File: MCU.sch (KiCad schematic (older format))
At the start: 46 parts, among them J12 Conn_02x05_Odd_Even, Q28 LBSS84LT1G, SW3 SW_Push, SW4 SW_Push, U10 ESP32-WROOM-32U, U16 CH340G, U6 STM32F730R8T6, U7 LY68L6400SLIT, U9 FS35ND01G-S1Y2QWFI000, Y1 Q13FC1350000400, Y2 24MHz, Y3 12MHz

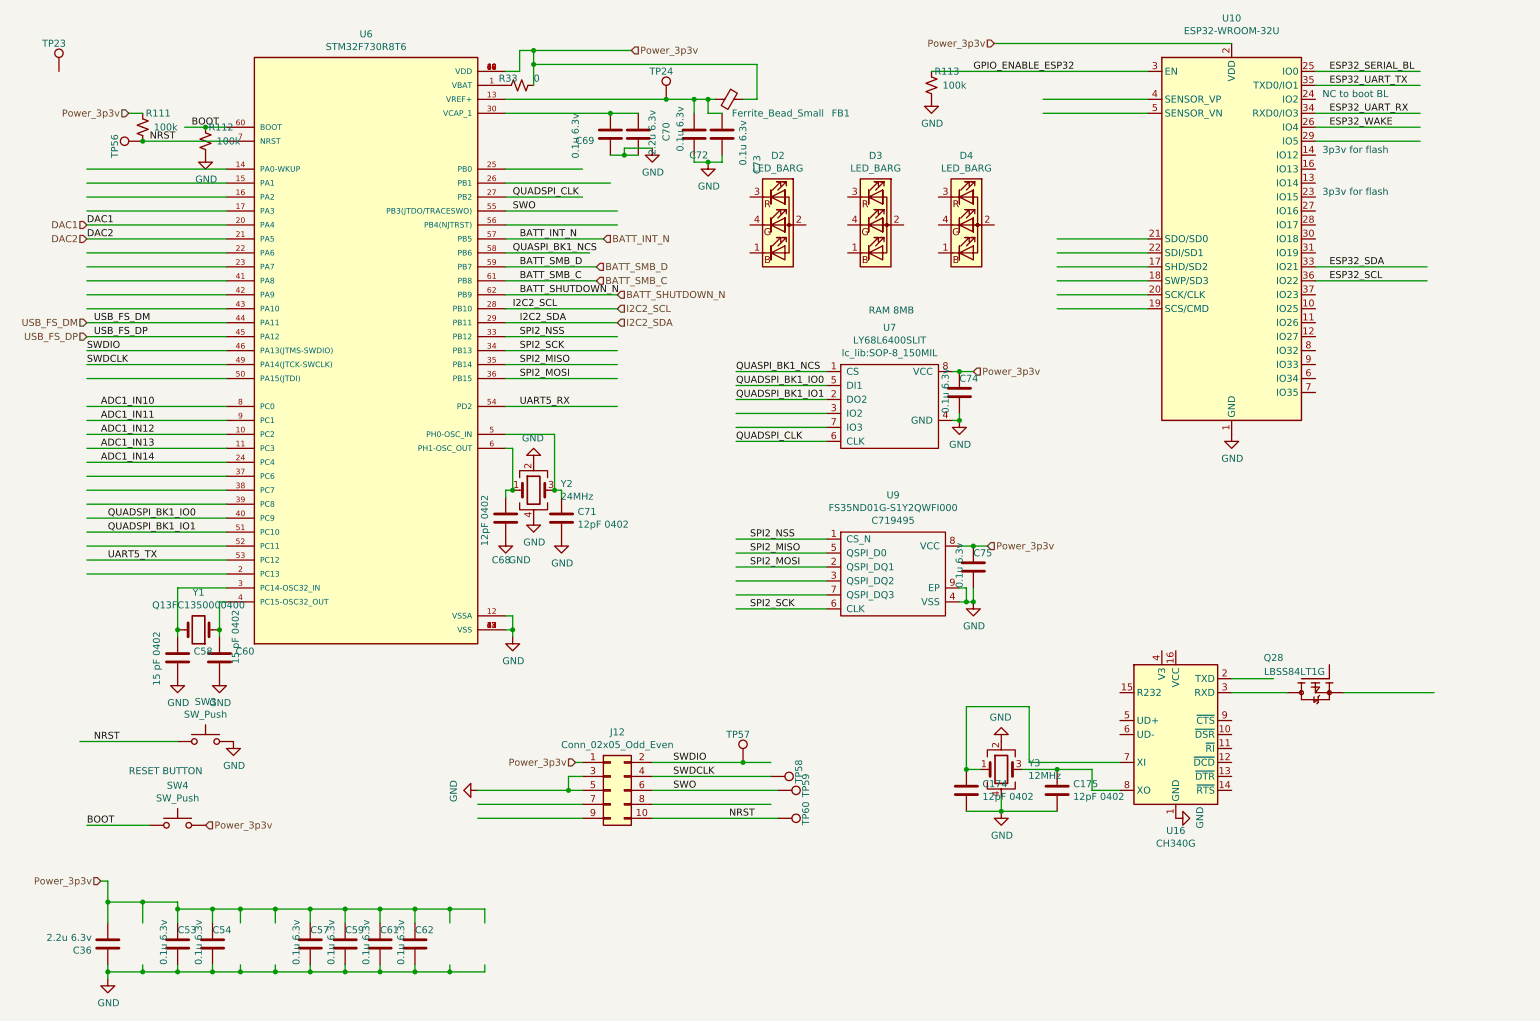
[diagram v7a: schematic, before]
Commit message: lots of GPIO connectivity changes. fixed no PD on input fixed CH340G leakage. can otherwise power from GPIO. added fet for powering VCONN from 3v/5v NEED TO ADD OVERCURRENT
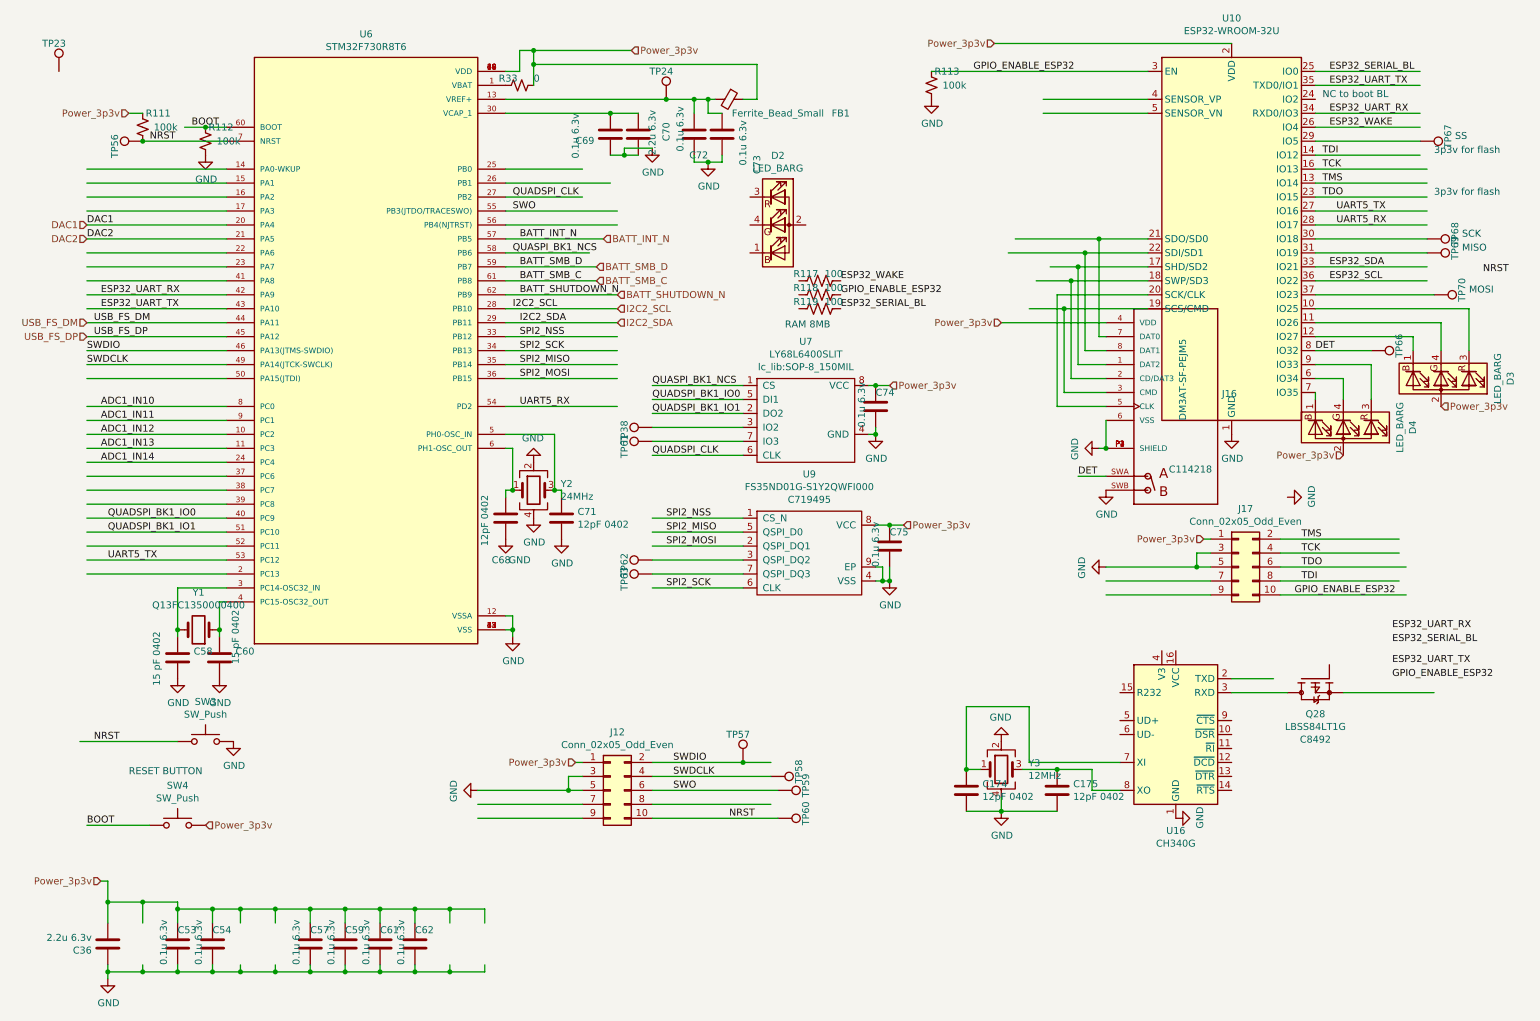
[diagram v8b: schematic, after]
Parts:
- removed Q28: LBSS84LT1G, lc_lib:SOT-23(SOT-23-3), symbol SmartBattery:VBA2625
- added J16: DM3AT-SF-PEJM5, SmartBattery:HRS_DM3AT-SF-PEJM5, symbol SmartBattery:DM3AT-SF-PEJM5
- added J17: Conn_02x05_Odd_Even, Connector_PinHeader_1.27mm:PinHeader_2x05_P1.27mm_Vertical_SMD, symbol Connector_Generic:Conn_02x05_Odd_Even
- added Q28: LBSS84LT1G, lc_lib:SOT-23(SOT-23-3), symbol SmartBattery:LBSS84LT1G
- added R117, R118, R119: 100, lc_lib:0402_R, symbol Device:R_US
- added TP38, TP61, TP62, TP63, TP66, TP67, TP68, TP69, TP70: TestPoint, TestPoint:TestPoint_Pad_D2.0mm, symbol Connector:TestPoint
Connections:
- net labels added: DET, TCK, TDI, TDO, TMS
- wire segments 214 -> 268
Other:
- note added: "3p3v for flash\n"
- note added: "MISO"
- note added: "MOSI"
- note added: "SCK"
- note added: "SS\n"
- moved on the sheet: C74, C75, D3, D4, U7, U9
